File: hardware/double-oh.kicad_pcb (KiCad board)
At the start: 2 copper layers, 81.6 x 14 mm, 54 parts, among them J1 USB_B_Micro, J10 Conn_01x01, J11 Conn_01x01, J12 Conn_01x01, J13 Conn_01x01, J2 Conn_01x01, J3 Conn_01x01, J4 Conn_01x01, J5 Conn_01x01, J6 Conn_01x01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

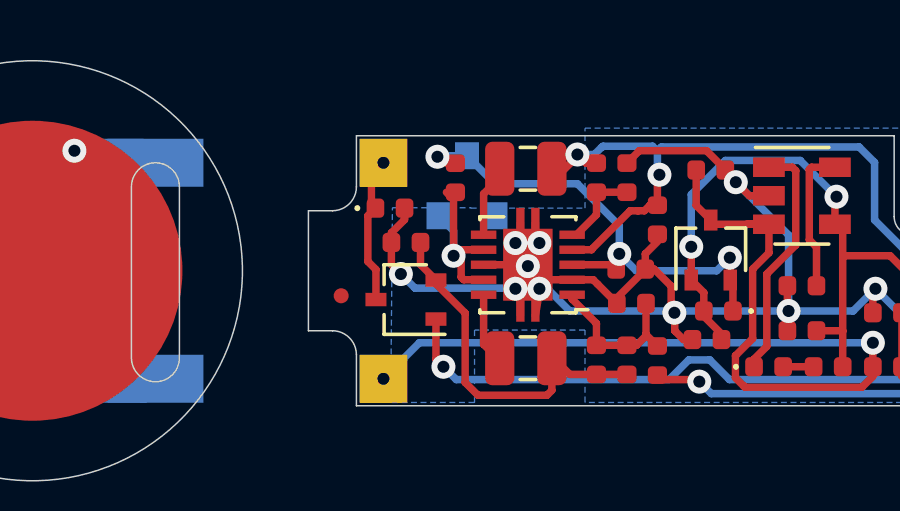
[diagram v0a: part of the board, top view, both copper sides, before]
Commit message: Clean up schematic, instructions, and BOM
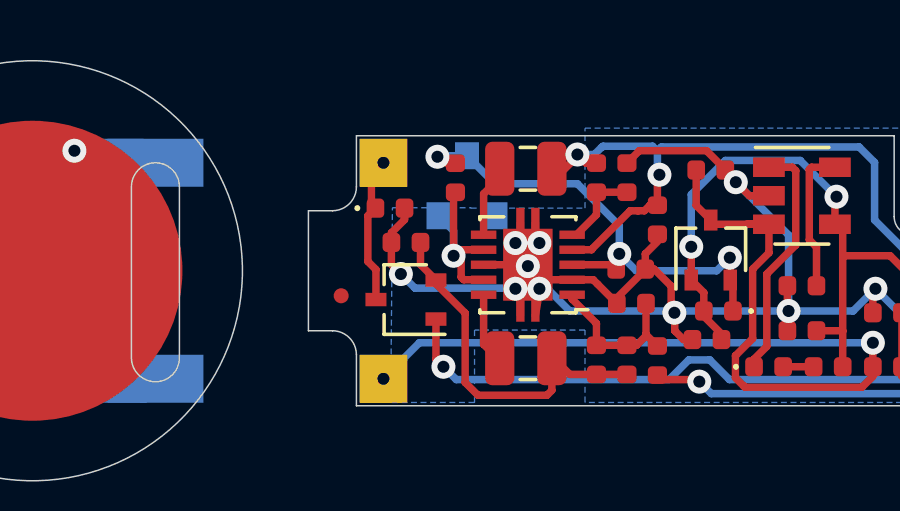
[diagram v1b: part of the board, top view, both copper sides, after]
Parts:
- C3: renamed from C5; value 0.1μF -> 4.7μF
- renumbered C10 to C4, C11 to C5, C13 to C6, C12 to C7, C7 to C8
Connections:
- AE1 pad 2: Net-(AE1-Pad2) -> (no net)
- J1 pad 4: Net-(J1-Pad4) -> (no net)
- J12 pad 1: Net-(J12-Pad1) -> (no net)
- J13 pad 1: Net-(J13-Pad1) -> (no net)
- U2 pad 1: Net-(U2-Pad1) -> (no net)
- U2 pad 10: Net-(U2-Pad10) -> (no net)
- U2 pad 11: Net-(U2-Pad11) -> (no net)
- U2 pad 12: Net-(U2-Pad12) -> (no net)
- U2 pad 13: Net-(U2-Pad13) -> (no net)
- U2 pad 14: Net-(U2-Pad14) -> (no net)
- U2 pad 15: Net-(U2-Pad15) -> (no net)
- U2 pad 16: Net-(U2-Pad16) -> (no net)
- U2 pad 17: Net-(U2-Pad17) -> (no net)
- U2 pad 18: Net-(U2-Pad18) -> (no net)
- U2 pad 22: Net-(U2-Pad22) -> (no net)
- U2 pad 24: Net-(U2-Pad24) -> (no net)
- U2 pad 9: Net-(U2-Pad9) -> (no net)
- U4 pad 10: Net-(U4-Pad10) -> (no net)
- U4 pad 11: Net-(U4-Pad11) -> (no net)
- U4 pad 15: Net-(U4-Pad15) -> (no net)
- U4 pad 16: Net-(U4-Pad16) -> (no net)
- U4 pad 17: Net-(U4-Pad17) -> (no net)
- U4 pad 18: Net-(U4-Pad18) -> (no net)
- U4 pad 20: Net-(U4-Pad20) -> (no net)
- U4 pad 21: Net-(U4-Pad21) -> (no net)
- U4 pad 22: Net-(U4-Pad22) -> (no net)
- U4 pad 25: Net-(U4-Pad25) -> (no net)
- U4 pad 26: Net-(U4-Pad26) -> (no net)
- U4 pad 27: Net-(U4-Pad27) -> (no net)
- U4 pad 28: Net-(U4-Pad28) -> (no net)
- U4 pad 29: Net-(U4-Pad29) -> (no net)
- U4 pad 30: Net-(U4-Pad30) -> (no net)
- U4 pad 31: Net-(U4-Pad31) -> (no net)
- U4 pad 32: Net-(U4-Pad32) -> (no net)
- U4 pad 33: Net-(U4-Pad33) -> (no net)
- U4 pad 34: Net-(U4-Pad34) -> (no net)
- U4 pad 35: Net-(U4-Pad35) -> (no net)
- U4 pad 36: Net-(U4-Pad36) -> (no net)
- U4 pad 38: Net-(U4-Pad38) -> (no net)
- U4 pad 42: Net-(U4-Pad42) -> (no net)
- U4 pad 44: Net-(U4-Pad44) -> (no net)
- U4 pad 45: Net-(U4-Pad45) -> (no net)
- U4 pad 47: Net-(U4-Pad47) -> (no net)
- U4 pad 48: Net-(U4-Pad48) -> (no net)
- U4 pad 5: Net-(U4-Pad5) -> (no net)
- U4 pad 6: Net-(U4-Pad6) -> (no net)
- U4 pad 7: Net-(U4-Pad7) -> (no net)
- U4 pad 8: Net-(U4-Pad8) -> (no net)
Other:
- rule pad_to_mask_clearance: 0.051 -> 0

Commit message: Might need to bump this to 3.0 soon
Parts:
- removed L2, L3: 2.2μH, double-oh:L_0806_2016Metric
- removed R5: 470kΩ, Resistor_SMD:R_0402_1005Metric
- added C9: 10μF, Capacitor_SMD:C_0402_1005Metric, F.Cu at (101.5, 103.6)
- added U6: TPSM828x, double-oh:microSiL-10, F.Cu at (107.1, 107.3)
- C4: value 10μF -> 4.7μF
- C6: value 10μF -> 120pF
- C7: value 33pF -> 4.7μF
- R10: value 120kΩ -> 68kΩ
- R11: value 330kΩ -> 68kΩ
- R9: value 470kΩ -> 330kΩ
- U3: value TPS62400 -> TPSM828x; footprint Package_SON:VSON-10-1EP_3x3mm_P0.5mm_EP1.65x2.4mm -> double-oh:microSiL-10
- U5: value BD48KxxG -> XC6120CxxxHR; footprint Package_TO_SOT_SMD:SOT-23 -> double-oh:USP-3; moved to F.Cu
- moved R9 7.19 mm to (103.9, 107.3)
- moved C5 6.24 mm to (103.1, 102.9), turned to 270 degrees
- moved R6 6.22 mm to (104.4, 101.6), turned to 0 degrees
- moved R10 5.81 mm to (104.8, 105.4), turned to 0 degrees
- moved U5 5.32 mm to (109.0, 102.0)
- moved C6 5.02 mm to (105.0, 107.3), turned to 270 degrees
- moved R2 3.91 mm to (117.1, 101.8), turned to 270 degrees
- moved R4 3.40 mm to (116.5, 104.4)
- moved D1 3.40 mm to (114.5, 104.4)
- moved C7 2.87 mm to (108.9, 104.6), turned to 0 degrees
- moved C4 1.39 mm to (108.9, 103.6), turned to 0 degrees
- moved C1 1.22 mm to (116.0, 106.1), turned to 90 degrees
- moved R11 1.20 mm to (109.2, 107.5)
- moved U3 0.95 mm to (105.2, 103.5), turned to 270 degrees
- moved Q3 0.72 mm to (111.3, 103.3)
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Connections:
- C4 pad 1: 0V -> TPS_VIN
- C4 pad 2: 3.3V -> 0V
- C5 pad 1: TPS_VIN -> 0V
- C5 pad 2: 0V -> 3.3V
- C6 pad 1: 0V -> batt_out
- C6 pad 2: batt_out -> DAC
- C7 pad 1: batt_out -> TPS_VIN
- C7 pad 2: DAC -> 0V
- R10 pad 1: 0V -> batt_out
- R11 pad 1: batt_out -> DAC
- R11 pad 2: DAC -> 0V
- R6 pad 1: DAC -> 3.3V
- R6 pad 2: 0V -> Net-(R6-Pad2)
- R9 pad 1: 3.3V -> batt_out
- R9 pad 2: Net-(R10-Pad2) -> DAC
- U3 pad 1: DAC -> TPS_VIN
- U3 pad 10: Net-(L3-Pad1) -> 0V
- U3 pad 2: 0V -> TPS_VIN
- U3 pad 3: TPS_VIN -> TPS_EN
- U3 pad 4: 3.3V -> Net-(R6-Pad2)
- U3 pad 5: Net-(R10-Pad2) -> 3.3V
- U3 pad 6: Net-(L2-Pad1) -> 3.3V
- U3 pad 7: TPS_EN -> 3.3V
- U3 pad 8: 0V -> 3.3V
- U3 pad 9: TPS_EN -> 0V
- U5 pad 1: 0V -> TPS_VIN
- U5 pad 3: TPS_VIN -> 0V
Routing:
- net 0V: track 98.3 -> 79.0 mm, vias 26 -> 32
- net LIPO_V: track 33.1 -> 24.8 mm
- net batt_out: track 12.0 -> 6.32 mm
- net Net-(D1-Pad1): track 8.05 -> 4.47 mm
- net DAC: track 5.42 -> 8.76 mm
- net Net-(R2-Pad2): track 4.86 -> 1.86 mm
- net TPS_EN: track 6.30 -> 8.97 mm, vias 1 -> 2
- net TPS_VIN: track 16.4 -> 13.9 mm, vias 3 -> 2
- net Net-(L3-Pad1): track 2.42 -> 0.00 mm
- net Net-(L2-Pad1): track 2.13 -> 0.00 mm
- net 3.3V: track 57.5 -> 59.6 mm, vias 3 -> 2
- net USB_VIN: track 26.4 -> 24.5 mm
- net Net-(R12-Pad2): track 29.9 -> 31.4 mm
- net Net-(R6-Pad2): track 0.00 -> 1.36 mm
- net RTS: track 19.7 -> 20.8 mm
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- added copper zone on F.Cu, net 0V
- added copper zone on F.Cu, net 3.3V
- added copper zone on F.Cu, net TPS_VIN
- added copper zone on F.Cu, net batt_out
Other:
- net class Larger added: clearance 0.2, trace_width 0.4, via_dia 0.8, via_drill 0.4
- board text added: "Double-Oh v2.8 // July 2021"
- board text removed: "Double-Oh v2.7 // Sept. 2020"

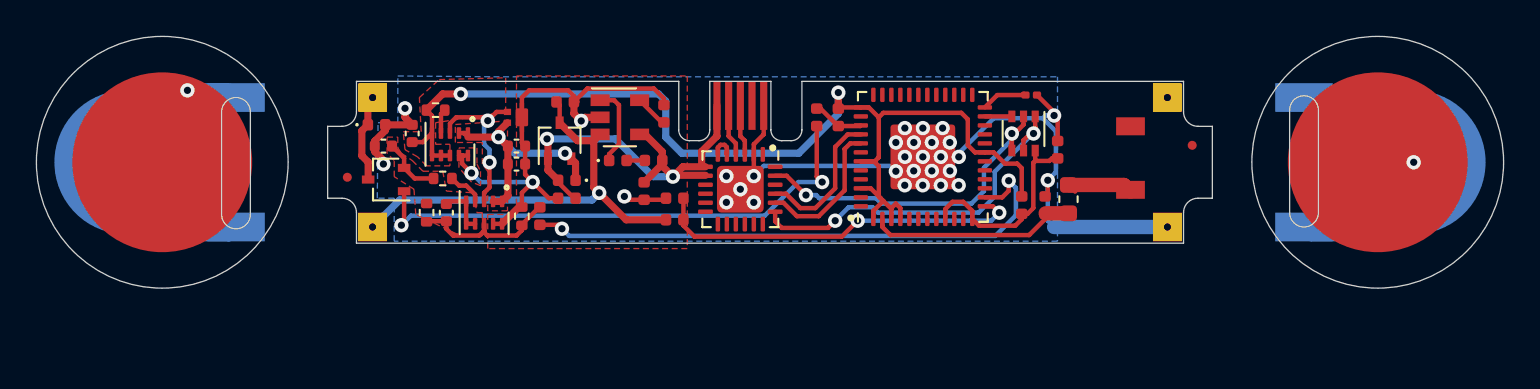
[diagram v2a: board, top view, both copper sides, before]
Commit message: Using Harwin Shield Finger as spring contact on anode now
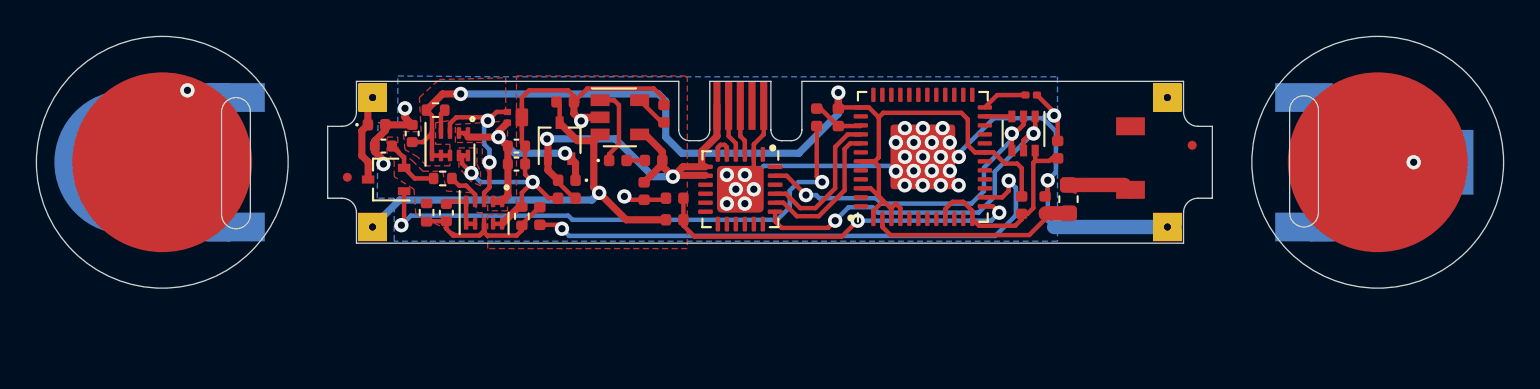
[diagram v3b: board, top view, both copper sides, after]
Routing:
- net Net-(Q2-Pad1): track 29.6 -> 30.3 mm
- net 0V: vias 32 -> 33

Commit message: Version 3 point oh!
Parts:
- added JP3: Jumper_NO_Small, double-oh:solder_bridge, F.Cu at (129.7, 107.5)
- JP1: footprint Resistor_SMD:R_0201_0603Metric -> double-oh:solder_bridge
- U4: value ESP32-PICO-D4 -> ESP32-U4WDH; footprint double-oh:QFN-48-1EP_7x7mm_P0.5mm_EP3.6x3.6mm -> Package_DFN_QFN:QFN-48-1EP_5x5mm_P0.35mm_EP3.7x3.7mm
- moved R8 2.25 mm to (126.2, 104.2)
- moved R7 0.65 mm to (126.2, 102.2)
- moved JP1 0.62 mm to (137.1, 101.2)
- moved U4 0.56 mm to (131.6, 103.7)
- moved Q1 0.45 mm to (137.1, 103.3)
- moved D2 0.38 mm to (101.5, 102.4)
- turned C9 to 180 degrees
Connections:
- net GPIO33 renamed ADC
- U4 pad 12: EN -> (no net)
- U4 pad 3: 3.3V -> Net-(JP3-Pad1)
- U4 pad 38: (no net) -> 3.3V
- U4 pad 4: 3.3V -> Net-(JP3-Pad1)
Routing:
- net 0V: track 79.0 -> 55.9 mm, vias 33 -> 28
- net Net-(JP3-Pad1): track 0.00 -> 2.89 mm
- net ADC: track 20.9 -> 23.6 mm
- net Net-(Q2-Pad1): track 30.3 -> 27.8 mm
- net DTR: track 19.4 -> 21.5 mm, vias 2 -> 0
- net batt_out: track 6.32 -> 4.84 mm
- net Net-(R7-Pad2): track 2.87 -> 4.25 mm
- net GPIO0: track 1.50 -> 2.78 mm
- net RTS: track 20.8 -> 19.7 mm
- net EN: track 11.5 -> 10.7 mm
- net 3.3V: track 59.6 -> 60.4 mm, vias 2 -> 4
- net RX_USB: track 8.10 -> 8.87 mm
- net RX_ESP: track 8.14 -> 8.78 mm
- net Net-(AE1-Pad1): track 4.13 -> 3.60 mm
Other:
- net class Default: trace_width 0.25 -> 0.2
- net class U4WDH added: clearance 0.14, trace_width 0.2, via_dia 0.8, via_drill 0.4
- board text added: "Double-Oh v3.0 // July 2021"
- board text removed: "Double-Oh v2.8 // July 2021"

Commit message: To be continued
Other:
- outline, holes or cut-outs redrawn

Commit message: working on condensing the board
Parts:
- added D4: RCLAMP1624T, double-oh:SLP1710P4T, F.Cu at (128.3, 111.2)
- U3, U6: value TPSM828x -> TPSM8282x
- moved U2 6.76 mm to (121.7, 112.8)
- moved R3 2.01 mm to (115.7, 106.7)
- moved R1 2.00 mm to (115.7, 107.8)
- moved C1 0.63 mm to (115.7, 105.5), turned to 0 degrees
- moved R6 0.46 mm to (104.7, 101.2), turned to 270 degrees
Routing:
- net USB_VIN: track 24.5 -> 16.3 mm
- net RX_ESP: track 8.78 -> 5.58 mm
- net RTS: track 19.7 -> 16.7 mm
- net Net-(D4-Pad2): track 2.88 -> 0.00 mm
- net RX_USB: track 8.87 -> 6.01 mm
- net Net-(D4-Pad3): track 2.82 -> 0.00 mm
- net 0V: track 55.9 -> 53.2 mm, vias 28 -> 22
- net 3.3V: track 60.4 -> 57.7 mm
- net DTR: track 21.5 -> 18.9 mm
- net LIPO_V: track 24.8 -> 23.4 mm
- net ADC: track 23.6 -> 24.8 mm
- net Net-(Q2-Pad1): track 27.8 -> 28.7 mm
- net TPS_EN: track 8.97 -> 9.77 mm

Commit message: bluh
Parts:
- removed D4: RCLAMP1624T, double-oh:SLP1710P4T
- removed JP3: Jumper_NO_Small, double-oh:solder_bridge
- removed the U4 at (131.6, 103.7)
- added U5: MCP73831-2-OT, Package_TO_SOT_SMD:SOT-23-5, F.Cu at (114.8, 102.2)
- U1: value MCP73831-2-OT -> ESP32-U4WDH; footprint Package_TO_SOT_SMD:SOT-23-5 -> Package_DFN_QFN:QFN-48-1EP_5x5mm_P0.35mm_EP3.7x3.7mm
- moved R3 18.5 mm to (134.2, 107.5)
- moved U1 17.6 mm to (132.2, 103.7), turned to 90 degrees
- moved R8 16.5 mm to (109.9, 101.8), turned to 90 degrees
- moved R6 16.1 mm to (119.5, 107.3)
- moved C5 15.0 mm to (117.8, 105.4), turned to 0 degrees
- moved R1 13.1 mm to (102.7, 107.0), turned to 270 degrees
- moved U3 12.7 mm to (117.4, 107.2), turned to 90 degrees
- moved C9 8.07 mm to (109.5, 105.0), turned to 270 degrees
- moved C4 7.36 mm to (115.2, 107.4), turned to 90 degrees
- moved Q2 6.84 mm to (107.4, 101.8), turned to 0 degrees
- moved U2 6.67 mm to (123.2, 106.2)
- moved U6 6.15 mm to (103.5, 104.8), turned to 180 degrees
- moved R12 5.90 mm to (105.6, 103.8), turned to 180 degrees
- moved R10 4.97 mm to (109.5, 107.2), turned to 270 degrees
- moved D1 4.75 mm to (118.5, 101.7), turned to 270 degrees
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- renumbered R14 to R5, U6 to U4, U5 to U6
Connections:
- U1 pad 1: Net-(D1-Pad1) -> 3.3V
- U1 pad 2: 0V -> Net-(C8-Pad2)
- U1 pad 3: LIPO_V -> 3.3V
- U1 pad 4: USB_VIN -> 3.3V
- U1 pad 5: Net-(R2-Pad2) -> (no net)
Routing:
- net Net-(Q2-Pad1): track 28.7 -> 3.57 mm, vias 2 -> 0
- net Net-(R7-Pad2): track 4.25 -> 26.9 mm, vias 0 -> 2
- net 0V: track 53.2 -> 34.2 mm, vias 22 -> 28
- net 3.3V: track 57.7 -> 42.6 mm, vias 4 -> 6
- net ADC: track 24.8 -> 36.5 mm
- net TPS_EN: track 9.77 -> 18.2 mm, vias 2 -> 0
- net LIPO_V: track 23.4 -> 19.3 mm
- net Net-(R12-Pad2): track 31.3 -> 35.1 mm
- net Net-(J1-Pad2): track 0.00 -> 3.27 mm
- net Net-(J1-Pad3): track 0.00 -> 3.21 mm
- net DAC: track 8.76 -> 5.64 mm
- net Net-(JP3-Pad1): track 2.89 -> 0.00 mm
- net to_top_cap: track 5.19 -> 7.85 mm
- net batt_out: track 4.84 -> 2.66 mm
- net USB_VIN: track 16.3 -> 18.4 mm, vias 2 -> 0
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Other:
- outline, holes or cut-outs redrawn

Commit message: nearing 3.0 RC
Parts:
- added R14: 24kΩ, Resistor_SMD:R_0402_1005Metric, F.Cu at (119.8, 105.3)
- added R15: 47kΩ, Resistor_SMD:R_0402_1005Metric, F.Cu at (119.8, 107.3)
- added R16: 68kΩ, Resistor_SMD:R_0402_1005Metric, F.Cu at (103.7, 106.4)
- D1: value LED_Small_ALT -> Blue LED
- D2, D3: footprint Diode_SMD:D_0402_1005Metric -> double-oh:SOD-993
- J1: value USB_B_Micro -> Unshielded USB Micro port
- Q1: value Q_DUAL_NPN_NPN_E1B1C2E2B2C1 -> MUN5213DW1
- U2: value CP2104 -> CP2102N
- U3: value TPSM8282x -> TPSM828214SILR
- U4: value TPSM8282x -> TPSM82821SILR
- U6: value XC6120CxxxHR -> XC6120C342HR-G
- moved R1 1.52 mm to (101.5, 106.0), turned to 90 degrees
- moved D3 1.04 mm to (113.5, 105.2)
- moved C4 1.00 mm to (114.2, 107.4)
- moved C5 1.00 mm to (116.8, 105.4)
- moved R5 1.00 mm to (115.0, 105.0)
- moved R6 1.00 mm to (118.5, 107.3)
- moved U3 1.00 mm to (116.4, 107.2)
- moved Q3 0.95 mm to (111.5, 106.6)
- moved C1 0.65 mm to (116.6, 103.8)
- moved C2 0.65 mm to (111.5, 102.7)
- moved D1 0.65 mm to (117.8, 101.7)
- moved R2 0.65 mm to (116.6, 101.7)
- moved R4 0.65 mm to (117.8, 103.8)
- moved U5 0.65 mm to (114.1, 102.2)
- moved D2 0.05 mm to (104.0, 102.1)
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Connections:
- net Net-(J1-Pad2) renamed /D-
- net Net-(J1-Pad3) renamed /D+
- Q1 pad 1: RTS -> DTR
- Q1 pad 2: DTR -> RTS
- Q1 pad 3: GPIO0 -> EN
- Q1 pad 4: DTR -> RTS
- Q1 pad 5: RTS -> DTR
- Q1 pad 6: EN -> GPIO0
- U2 pad 11: (no net) -> 0V
- U2 pad 8: USB_VIN -> /Vbus
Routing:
- net ADC: track 36.5 -> 39.2 mm
- net /Vbus: track 0.00 -> 2.52 mm
- net 0V: track 34.2 -> 36.8 mm
- net LIPO_V: track 19.3 -> 17.9 mm
- net TPS_EN: track 18.2 -> 17.2 mm
- net USB_VIN: track 18.4 -> 19.1 mm
